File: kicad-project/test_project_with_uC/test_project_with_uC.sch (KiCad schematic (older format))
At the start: 2 parts, among them U1 ATtiny2313-20SU, Y1 12M

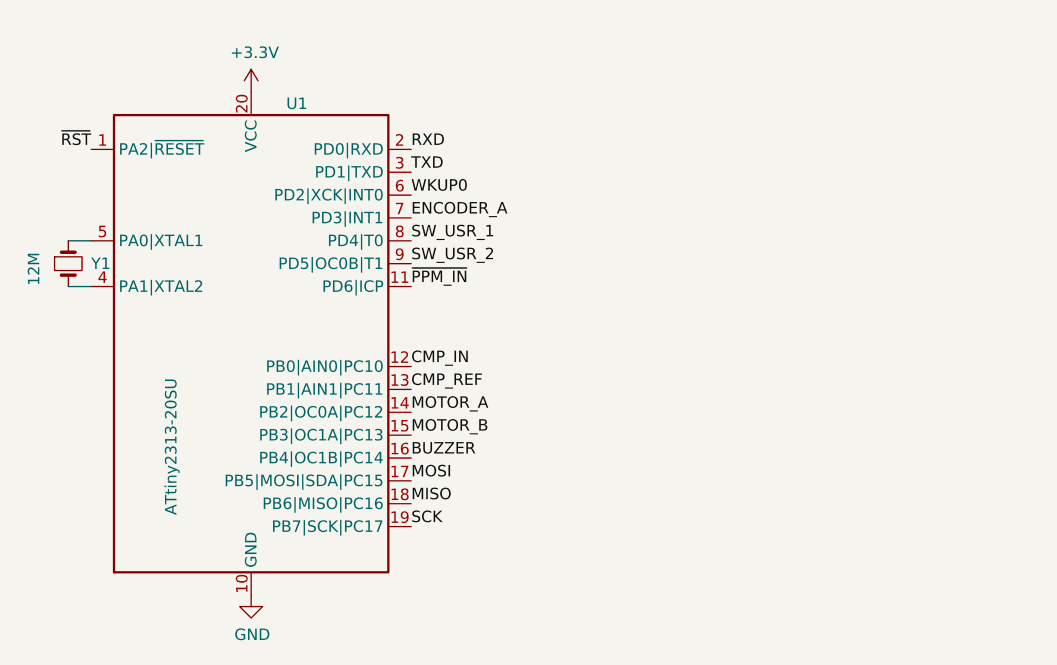
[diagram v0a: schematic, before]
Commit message: changed microcontroller symbol
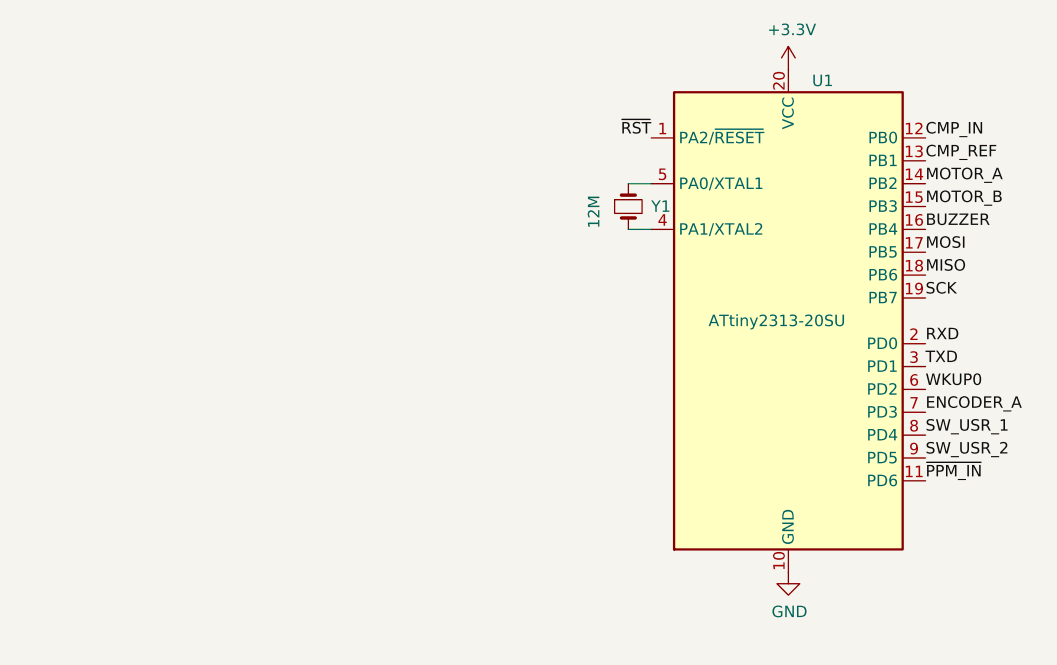
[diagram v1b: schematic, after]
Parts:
- removed U1: ATtiny2313-20SU, Package_SO:SOIC-20W_7.5x12.8mm_P1.27mm, symbol microcontrollers:ATtiny2313-20SU
- added U1: ATtiny2313-20SU, Package_SO:SOIC-20W_7.5x12.8mm_P1.27mm, symbol MCU_Microchip_ATtiny:ATtiny2313-20SU
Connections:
- net +3V3: now also U1.20 (VCC)
- net BUZZER: now also U1.16 (PB4)
- net CMP_IN: now also U1.12 (PB0)
- net CMP_REF: now also U1.13 (PB1)
- net ENCODER_A: now also U1.7 (PD3)
- net GND: now also U1.10 (GND)
- net MISO: now also U1.18 (PB6)
- net MOSI: now also U1.17 (PB5)
- net MOTOR_A: now also U1.14 (PB2)
- net MOTOR_B: now also U1.15 (PB3)
- net RXD: now also U1.2 (PD0)
- net SCK: now also U1.19 (PB7)
- net SW_USR_1: now also U1.8 (PD4)
- net SW_USR_2: now also U1.9 (PD5)
- net TXD: now also U1.3 (PD1)
- net WKUP0: now also U1.6 (PD2)
- net ~PPM_IN: now also U1.11 (PD6)
- net ~RST: now also U1.1 (PA2/~RESET)
- net at Y1.2: now also U1.4 (PA1/XTAL2)
- net at Y1.1: now also U1.5 (PA0/XTAL1)
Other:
- moved on the sheet: Y1
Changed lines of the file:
@@
 Comment4 ""
 $EndDescr
-$Comp
-L microcontrollers:ATtiny2313-20SU U1
-U 1 1 5CEBAACE
-P 3650 3200
-F 0 "U1" H 3850 4250 50  0000 C CNN
-F 1 "ATtiny2313-20SU" V 3300 2750 50  0000 C CNN
-F 2 "Package_SO:SOIC-20W_7.5x12.8mm_P1.27mm" H 4050 4950 50  0001 C CIN
-F 3 "http://ww1.microchip.com/downloads/en/DeviceDoc/Atmel-2543-AVR-ATtiny2313_Datasheet.pdf" H 3650 3200 50  0001 C CNN
-	1    3650 3200
-	1    0    0    -1
-$EndComp
-Text Label 4350 2350 0    50   ~ 0
+Text Label 6600 3800 0    50   ~ 0
+~PPM_IN
+Text Label 6600 3700 0    50   ~ 0
+SW_USR_2
+Text Label 6600 3600 0    50   ~ 0
+SW_USR_1
+Text Label 6600 3500 0    50   ~ 0
+ENCODER_A
+Text Label 6600 3400 0    50   ~ 0
+WKUP0
+Text Label 6600 3300 0    50   ~ 0
+TXD
+Text Label 6600 3200 0    50   ~ 0
 RXD
-Text Label 4350 2450 0    50   ~ 0
-TXD
-Text Label 4350 2550 0    50   ~ 0
-WKUP0
-Text Label 4350 2650 0    50   ~ 0
-ENCODER_A
-Text Label 4350 2750 0    50   ~ 0
-SW_USR_1
-Text Label 4350 2850 0    50   ~ 0
-SW_USR_2
-Text Label 4350 2950 0    50   ~ 0
-~PPM_IN
-Text Label 4350 3300 0    50   ~ 0
+Text Label 6600 3000 0    50   ~ 0
+SCK
+Text Label 6600 2900 0    50   ~ 0
+MISO
+Text Label 6600 2800 0    50   ~ 0
+MOSI
+Text Label 6600 2700 0    50   ~ 0
+BUZZER
+Text Label 6600 2600 0    50   ~ 0
+MOTOR_B
+Text Label 6600 2500 0    50   ~ 0
+MOTOR_A
+Text Label 6600 2400 0    50   ~ 0
+CMP_REF
+Text Label 6600 2300 0    50   ~ 0
 CMP_IN
-Text Label 4350 3400 0    50   ~ 0
-CMP_REF
-Text Label 4350 3500 0    50   ~ 0
-MOTOR_A
-Text Label 4350 3600 0    50   ~ 0
-MOTOR_B
-Text Label 4350 3700 0    50   ~ 0
-BUZZER
-Text Label 4350 3800 0    50   ~ 0
-MOSI
-Text Label 4350 3900 0    50   ~ 0
-MISO
-Text Label 4350 4000 0    50   ~ 0
-SCK
 $Comp
 L power:GND #PWR0101
 U 1 1 5CEBBE3A
-P 3650 4300
-F 0 "#PWR0101" H 3650 4050 50  0001 C CNN
-F 1 "GND" H 3655 4127 50  0000 C CNN
-F 2 "" H 3650 4300 50  0001 C CNN
-F 3 "" H 3650 4300 50  0001 C CNN
-	1    3650 4300
+P 6000 4200
+F 0 "#PWR0101" H 6000 3950 50  0001 C CNN
+F 1 "GND" H 6005 4027 50  0000 C CNN
+F 2 "" H 6000 4200 50  0001 C CNN
+F 3 "" H 6000 4200 50  0001 C CNN
+	1    6000 4200
 	1    0    0    -1
 $EndComp
@@
 L power:+3.3V #PWR0102
 U 1 1 5CEBDE39
-P 3650 2100
-F 0 "#PWR0102" H 3650 1950 50  0001 C CNN
-F 1 "+3.3V" H 3665 2273 50  0000 C CNN
-F 2 "" H 3650 2100 50  0001 C CNN
-F 3 "" H 3650 2100 50  0001 C CNN
-	1    3650 2100
+P 6000 2000
+F 0 "#PWR0102" H 6000 1850 50  0001 C CNN
+F 1 "+3.3V" H 6015 2173 50  0000 C CNN
+F 2 "" H 6000 2000 50  0001 C CNN
+F 3 "" H 6000 2000 50  0001 C CNN
+	1    6000 2000
 	1    0    0    -1
 $EndComp
-Text Label 2950 2350 2    50   ~ 0
-~RST
+Wire Wire Line
+	5400 2700 5300 2700
+Wire Wire Line
+	5300 2500 5400 2500
 $Comp
 L Device:Crystal_Small Y1
 U 1 1 5CEBF29F
-P 2850 2850
-F 0 "Y1" V 2850 2950 50  0000 L CNN
-F 1 "12M" H 2800 2700 50  0000 L CNN
-F 2 "Crystal:Crystal_SMD_0603-4Pin_6.0x3.5mm" H 2850 2850 50  0001 C CNN
-F 3 "~" H 2850 2850 50  0001 C CNN
-	1    2850 2850
+P 5300 2600
+F 0 "Y1" V 5300 2700 50  0000 L CNN
+F 1 "12M" H 5250 2450 50  0000 L CNN
+F 2 "Crystal:Crystal_SMD_0603-4Pin_6.0x3.5mm" H 5300 2600 50  0001 C CNN
+F 3 "~" H 5300 2600 50  0001 C CNN
+	1    5300 2600
 	0    1    1    0
 $EndComp
-Wire Wire Line
-	2850 2750 2950 2750
-Wire Wire Line
-	2950 2950 2850 2950
+Text Label 5400 2300 2    50   ~ 0
+~RST
+$Comp
+L MCU_Microchip_ATtiny:ATtiny2313-20SU U1
+U 1 1 5CEE678D
+P 6000 3100
+F 0 "U1" H 6150 4150 50  0000 C CNN
+F 1 "ATtiny2313-20SU" H 5950 3100 50  0000 C CNN
+F 2 "Package_SO:SOIC-20W_7.5x12.8mm_P1.27mm" H 6000 3100 50  0001 C CIN
+F 3 "http://ww1.microchip.com/downloads/en/DeviceDoc/Atmel-2543-AVR-ATtiny2313_Datasheet.pdf" H 6000 3100 50  0001 C CNN
+	1    6000 3100
+	1    0    0    -1
+$EndComp
 $EndSCHEMATC

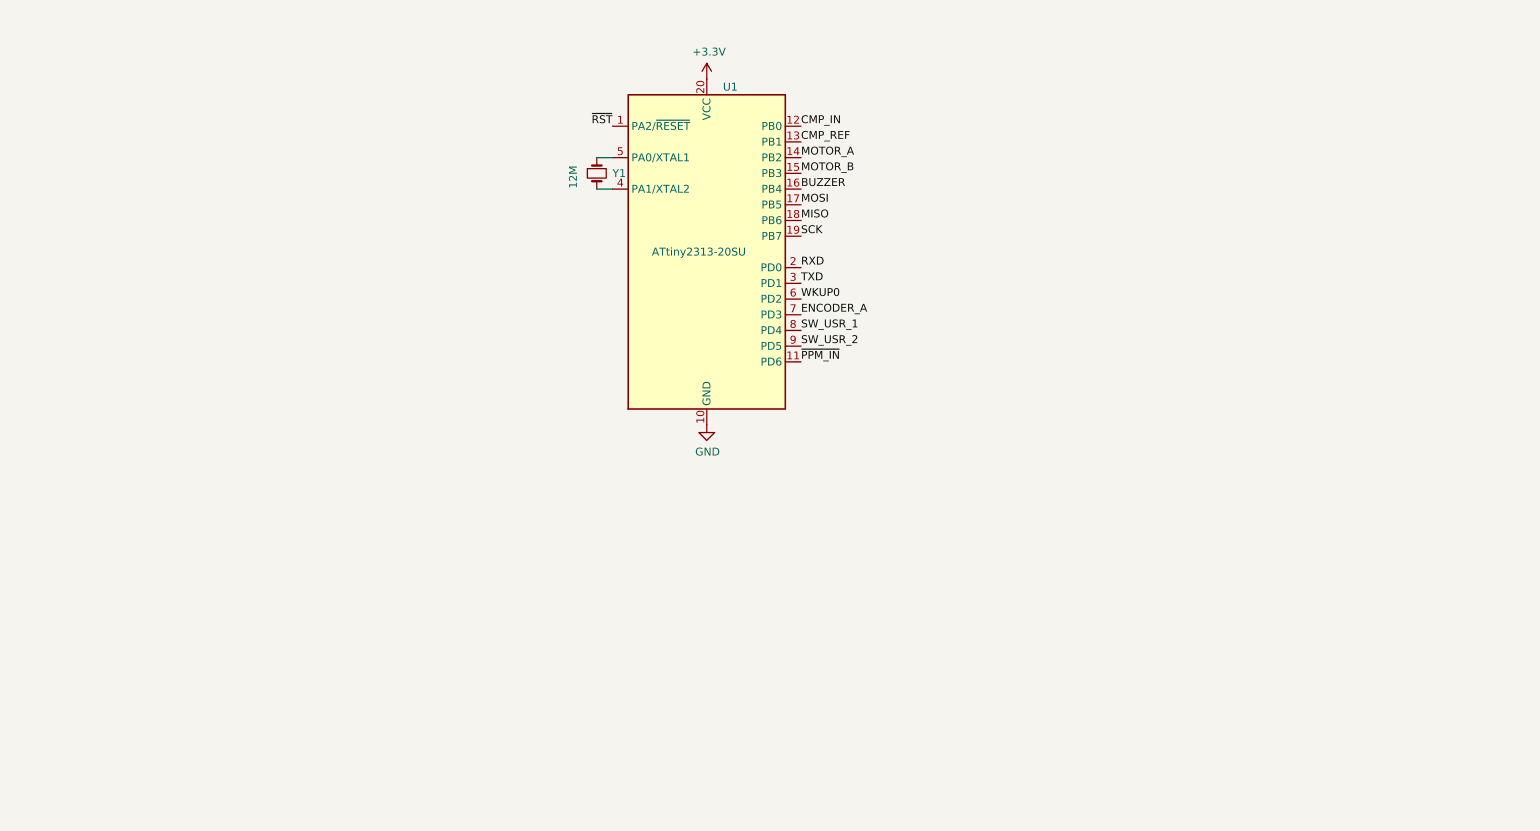
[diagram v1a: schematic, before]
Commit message: add another microcontroller, for real world scene
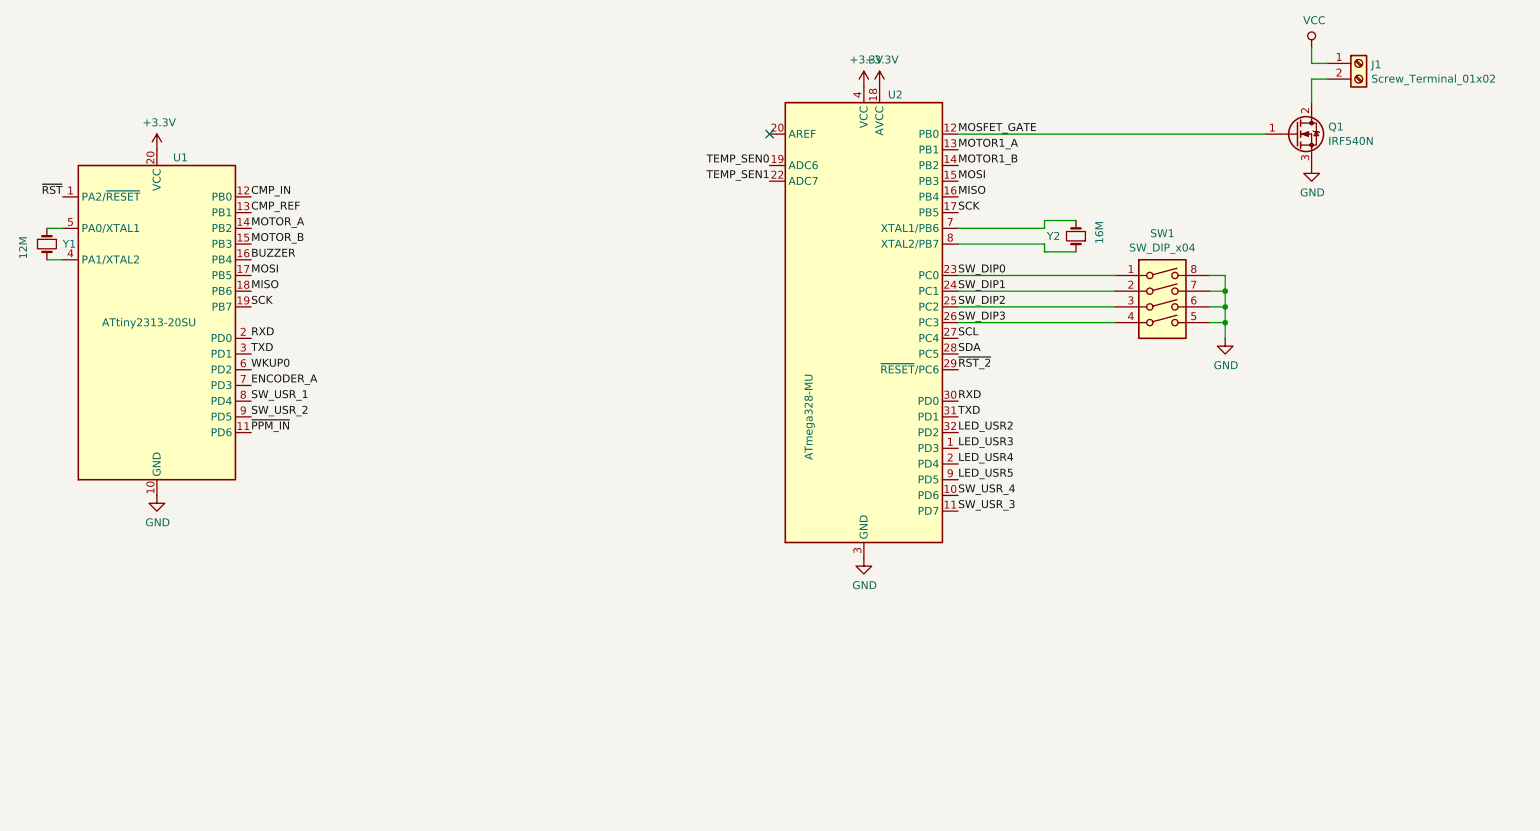
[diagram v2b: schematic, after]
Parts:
- added J1: Screw_Terminal_01x02, symbol Connector:Screw_Terminal_01x02
- added Q1: IRF540N, Package_TO_SOT_THT:TO-220-3_Vertical, symbol Transistor_FET:IRF540N
- added SW1: SW_DIP_x04, symbol Switch:SW_DIP_x04
- added U2: ATmega328-MU, Package_DFN_QFN:QFN-32-1EP_5x5mm_P0.5mm_EP3.1x3.1mm, symbol MCU_Microchip_ATmega:ATmega328-MU
- added Y2: 16M, Crystal:Crystal_SMD_0603-4Pin_6.0x3.5mm, symbol Device:Crystal_Small
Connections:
- net +3V3: now also U2.18 (AVCC), U2.4 (VCC), U2.6 (VCC)
- net GND: now also Q1.3 (S), SW1.5, SW1.6, SW1.7, SW1.8, U2.21 (GND), U2.3 (GND), U2.33 (GND), U2.5 (GND)
- net MISO: now also U2.16 (PB4)
- net MOSI: now also U2.15 (PB3)
- net RXD: now also U2.30 (PD0)
- net SCK: now also U2.17 (PB5)
- net TXD: now also U2.31 (PD1)
- new net: U2.7 (XTAL1/PB6), Y2.2
- new net: U2.8 (XTAL2/PB7), Y2.1
- new net: J1.2 (Pin_2), Q1.2 (D)
- new net LED_USR2: U2.32 (PD2)
- new net LED_USR3: U2.1 (PD3)
- new net LED_USR4: U2.2 (PD4)
- new net LED_USR5: U2.9 (PD5)
- new net MOSFET_GATE: Q1.1 (G), U2.12 (PB0)
- new net MOTOR1_A: U2.13 (PB1)
- new net MOTOR1_B: U2.14 (PB2)
- new net SCL: U2.27 (PC4)
- new net SDA: U2.28 (PC5)
- new net SW_DIP0: SW1.1, U2.23 (PC0)
- new net SW_DIP1: SW1.2, U2.24 (PC1)
- new net SW_DIP2: SW1.3, U2.25 (PC2)
- new net SW_DIP3: SW1.4, U2.26 (PC3)
- new net SW_USR_3: U2.11 (PD7)
- new net SW_USR_4: U2.10 (PD6)
- new net TEMP_SEN0: U2.19 (ADC6)
- new net TEMP_SEN1: U2.22 (ADC7)
- new net VCC: J1.1 (Pin_1)
- new net ~RST_2: U2.29 (~RESET~/PC6)
- no-connect marks 0 -> 1
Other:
- moved on the sheet: U1, Y1

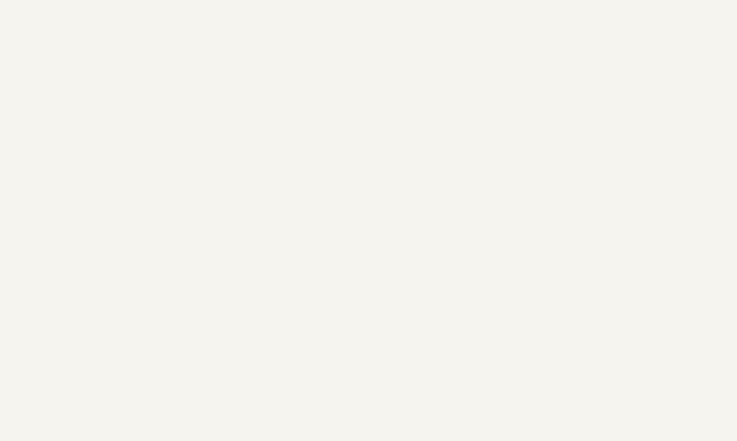
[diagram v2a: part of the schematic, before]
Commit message: add more parts to the sch for testing
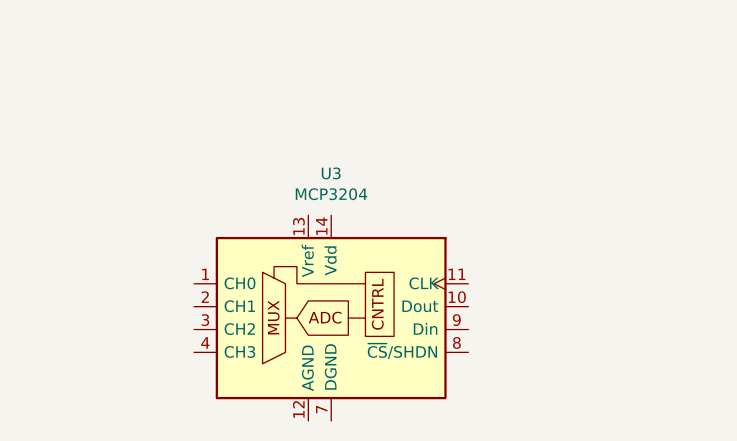
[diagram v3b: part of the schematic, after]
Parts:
- added U3: MCP3204, symbol Analog_ADC:MCP3204
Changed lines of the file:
@@
 Text Label 7600 3550 0    50   ~ 0
 SW_DIP3
+$Comp
+L Analog_ADC:MCP3204 U3
+U 1 1 5D50E6C3
+P 2950 6200
+F 0 "U3" H 2950 6781 50  0000 C CNN
+F 1 "MCP3204" H 2950 6690 50  0000 C CNN
+F 2 "" H 3850 5900 50  0001 C CNN
+F 3 "http://ww1.microchip.com/downloads/en/DeviceDoc/21298c.pdf" H 3850 5900 50  0001 C CNN
+	1    2950 6200
+	1    0    0    -1
+$EndComp
 $EndSCHEMATC

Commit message: testing with different order of input list
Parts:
- renumbered U1 to U2, U2 to U6
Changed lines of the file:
@@
 ~RST
 $Comp
-L MCU_Microchip_ATtiny:ATtiny2313-20SU U1
+L MCU_Microchip_ATtiny:ATtiny2313-20SU U2
 U 1 1 5CEE678D
 P 2500 3550
-F 0 "U1" H 2650 4600 50  0000 C CNN
+F 0 "U2" H 2650 4600 50  0000 C CNN
 F 1 "ATtiny2313-20SU" H 2450 3550 50  0000 C CNN
 F 2 "Package_SO:SOIC-20W_7.5x12.8mm_P1.27mm" H 2500 3550 50  0001 C CIN
@@
 $EndComp
 $Comp
-L MCU_Microchip_ATmega:ATmega328-MU U2
+L MCU_Microchip_ATmega:ATmega328-MU U6
 U 1 1 5CEEC004
 P 7000 3550
-F 0 "U2" H 7200 5000 50  0000 C CNN
+F 0 "U6" H 7200 5000 50  0000 C CNN
 F 1 "ATmega328-MU" V 6650 2950 50  0000 C CNN
 F 2 "Package_DFN_QFN:QFN-32-1EP_5x5mm_P0.5mm_EP3.1x3.1mm" H 7000 3550 50  0001 C CIN

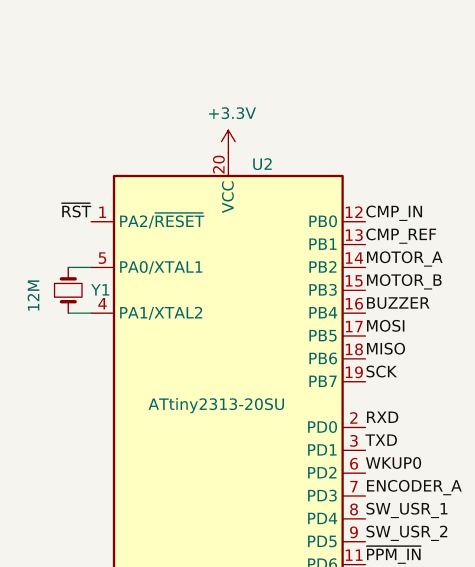
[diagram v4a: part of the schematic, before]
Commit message: changed KiCAD files to include XTAL for testing
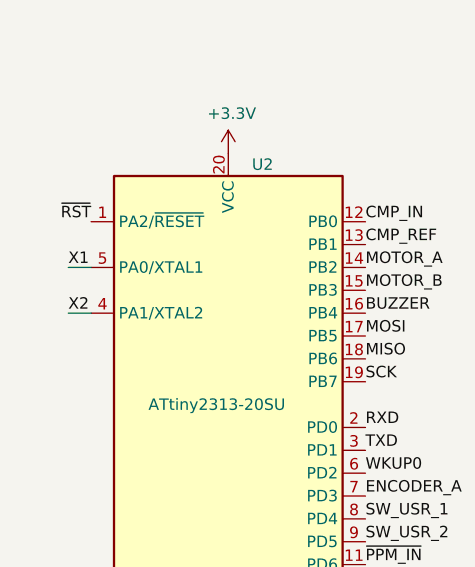
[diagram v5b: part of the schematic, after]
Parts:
- removed Y1: 12M, Crystal:Crystal_SMD_0603-4Pin_6.0x3.5mm, symbol Device:Crystal_Small
- U2: header (none) -> header/t2313_hw.h
- U6: header (none) -> headers/m328_hw.h
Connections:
- net X1: now reaches U2.5 (PA0/XTAL1)
- net X2: now reaches U2.4 (PA1/XTAL2)
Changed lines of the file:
@@
 Wire Wire Line
 	1800 2950 1900 2950
-$Comp
-L Device:Crystal_Small Y1
-U 1 1 5CEBF29F
-P 1800 3050
-F 0 "Y1" V 1800 3150 50  0000 L CNN
-F 1 "12M" H 1750 2900 50  0000 L CNN
-F 2 "Crystal:Crystal_SMD_0603-4Pin_6.0x3.5mm" H 1800 3050 50  0001 C CNN
-F 3 "~" H 1800 3050 50  0001 C CNN
-	1    1800 3050
-	0    1    1    0
-$EndComp
 Text Label 1900 2750 2    50   ~ 0
 ~RST
@@
 F 2 "Package_SO:SOIC-20W_7.5x12.8mm_P1.27mm" H 2500 3550 50  0001 C CIN
 F 3 "http://ww1.microchip.com/downloads/en/DeviceDoc/Atmel-2543-AVR-ATtiny2313_Datasheet.pdf" H 2500 3550 50  0001 C CNN
+F 4 "header/t2313_hw.h" H 2500 3550 50  0001 C CNN "header"
 	1    2500 3550
 	1    0    0    -1
@@
 F 2 "Package_DFN_QFN:QFN-32-1EP_5x5mm_P0.5mm_EP3.1x3.1mm" H 7000 3550 50  0001 C CIN
 F 3 "http://ww1.microchip.com/downloads/en/DeviceDoc/ATmega328_P%20AVR%20MCU%20with%20picoPower%20Technology%20Data%20Sheet%2040001984A.pdf" H 7000 3550 50  0001 C CNN
+F 4 "headers/m328_hw.h" H 7000 3550 50  0001 C CNN "header"
 	1    7000 3550
 	1    0    0    -1
@@
 	1    0    0    -1
 $EndComp
+Text Label 1800 2950 0    50   ~ 0
+X1
+Text Label 1800 3150 0    50   ~ 0
+X2
 $EndSCHEMATC

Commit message: Kicad save
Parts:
- U6: header headers/m328_hw.h -> header/m328_hw.h
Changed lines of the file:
@@
 F 2 "Package_DFN_QFN:QFN-32-1EP_5x5mm_P0.5mm_EP3.1x3.1mm" H 7000 3550 50  0001 C CIN
 F 3 "http://ww1.microchip.com/downloads/en/DeviceDoc/ATmega328_P%20AVR%20MCU%20with%20picoPower%20Technology%20Data%20Sheet%2040001984A.pdf" H 7000 3550 50  0001 C CNN
-F 4 "headers/m328_hw.h" H 7000 3550 50  0001 C CNN "header"
+F 4 "header/m328_hw.h" H 7000 3550 50  0001 C CNN "header"
 	1    7000 3550
 	1    0    0    -1
